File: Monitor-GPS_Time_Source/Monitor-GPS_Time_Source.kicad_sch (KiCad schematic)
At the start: 10 parts, among them J1 Conn_ARM_JTAG_SWD_10, J2 Conn_01x10_Pin, J3 Conn_01x10_Pin, SW1 SW_Omron_B3FS, U1 MSPM0C1105

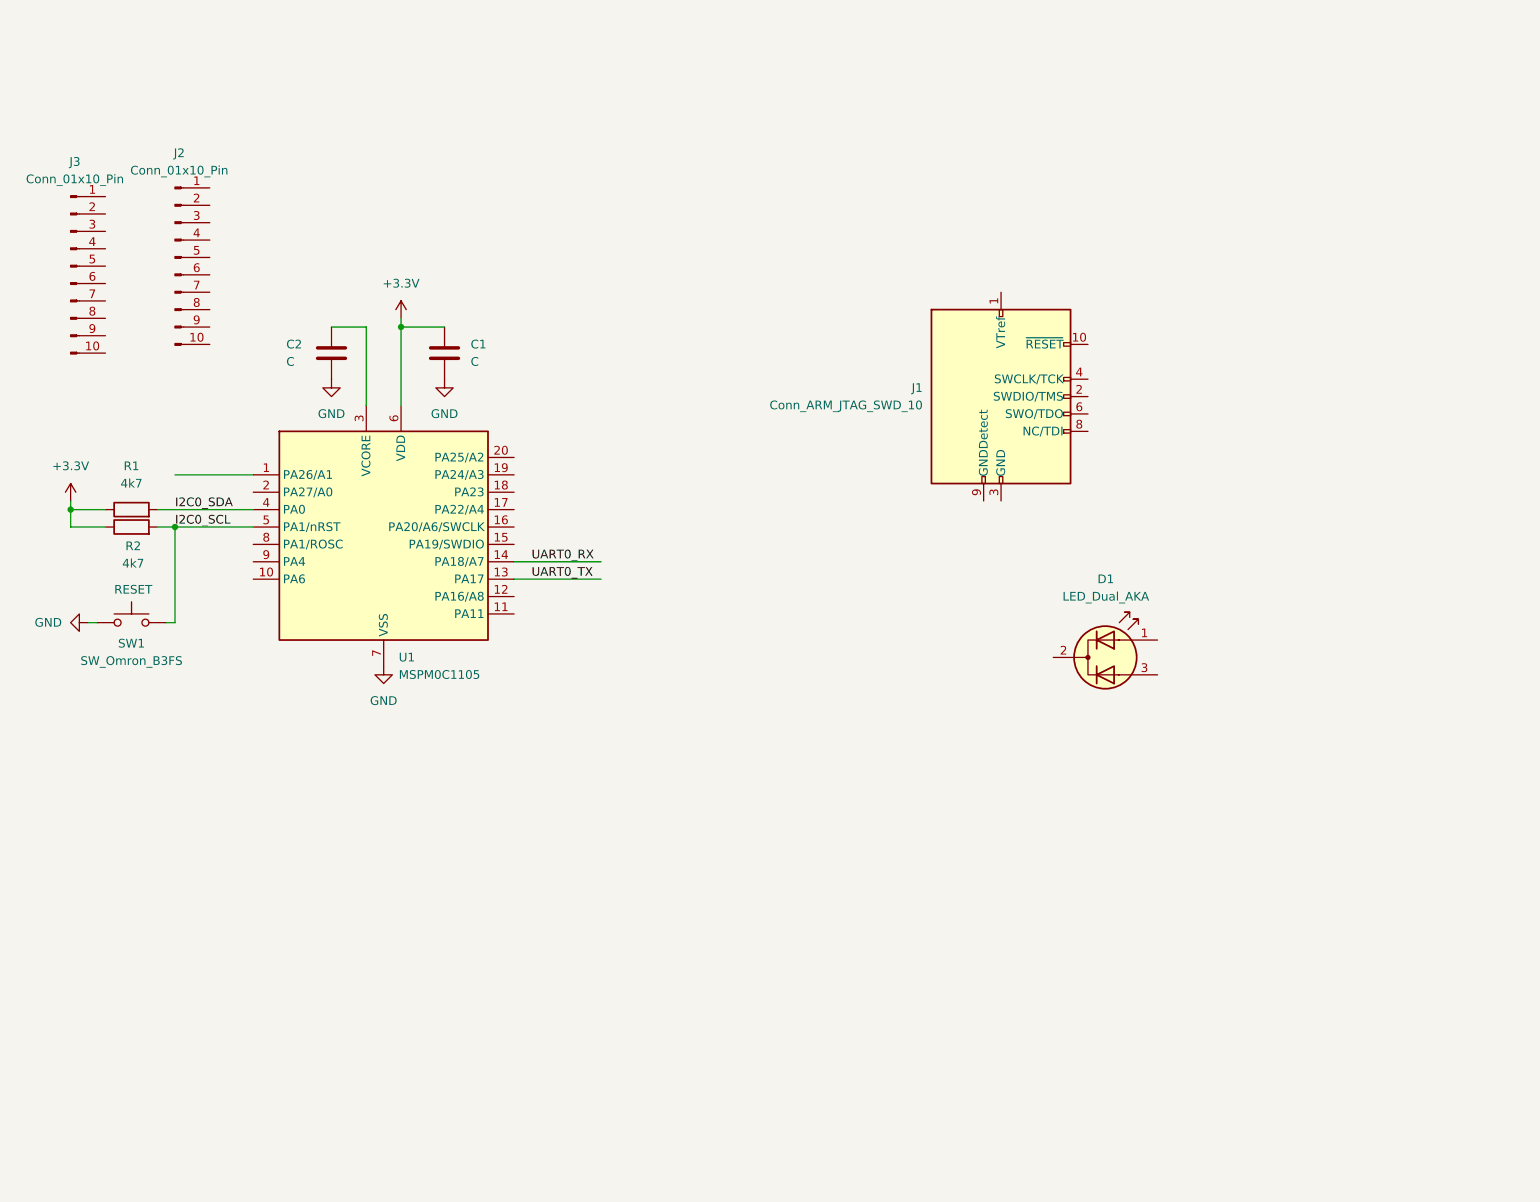
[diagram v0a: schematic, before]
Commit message: PCB layout complete, needs silkscreen work
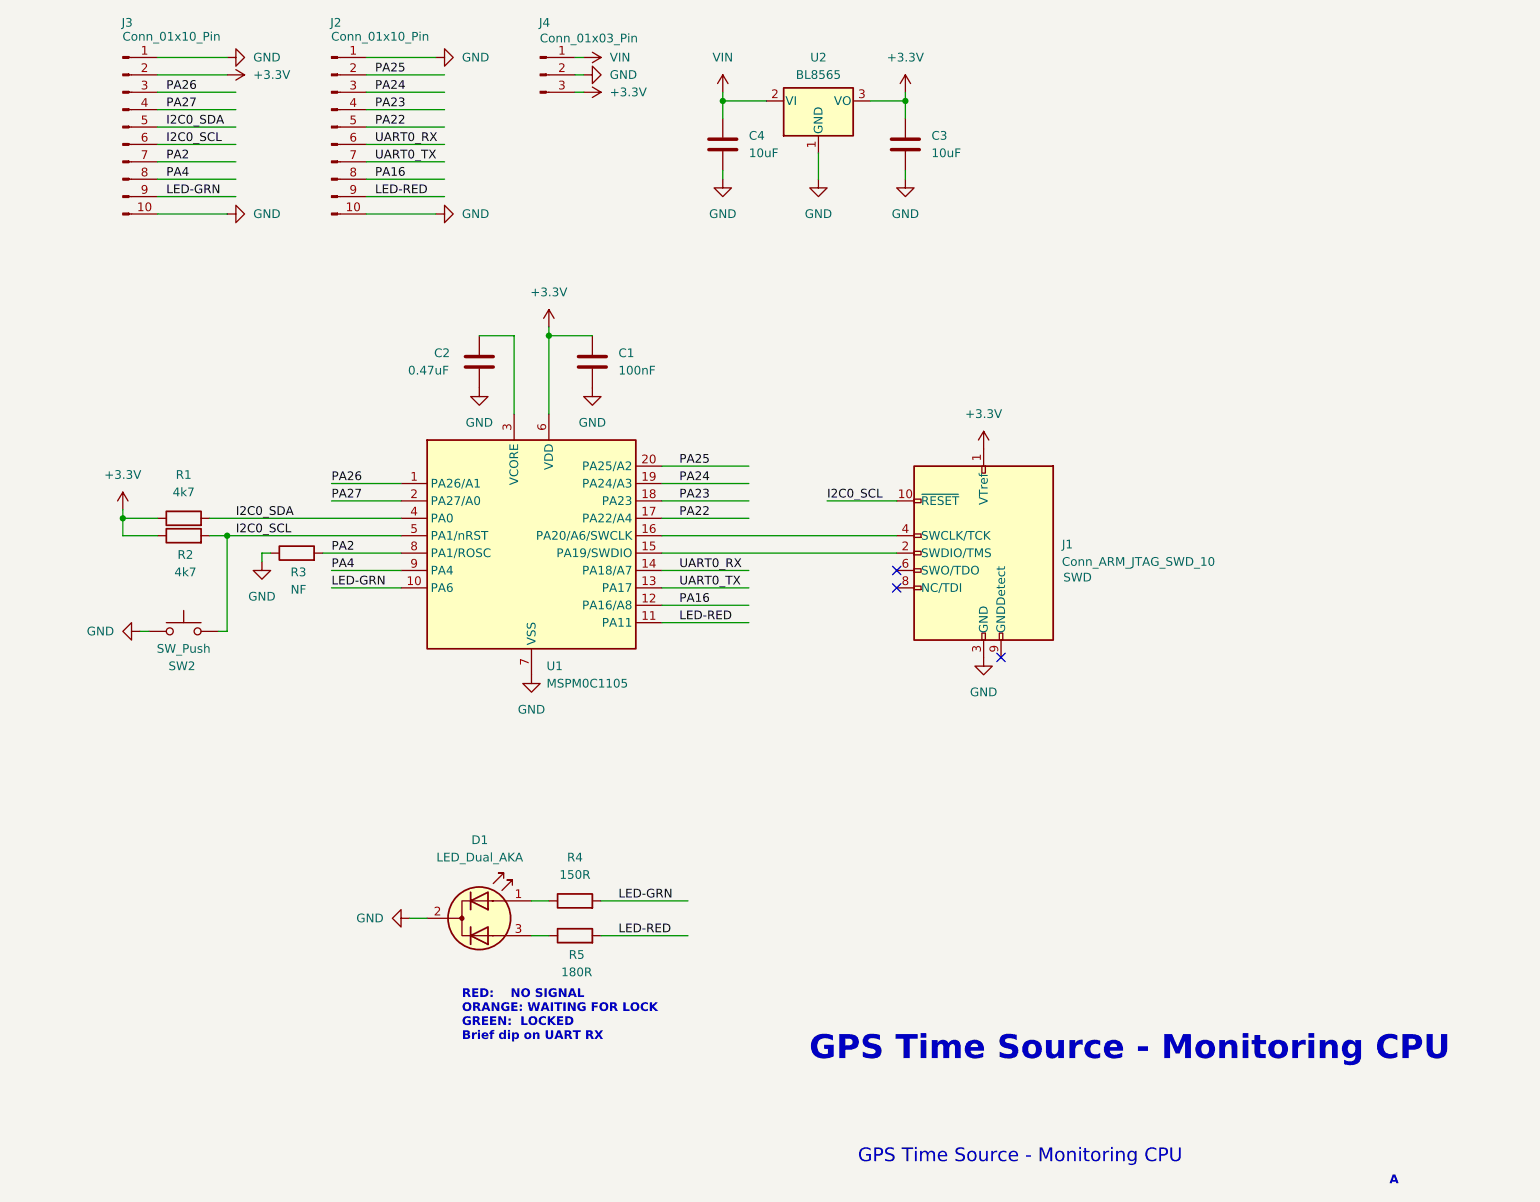
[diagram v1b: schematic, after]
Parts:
- removed SW1: SW_Omron_B3FS, Button_Switch_SMD:SW_SPST_Omron_B3FS-100xP, symbol Switch:SW_Omron_B3FS
- added C3, C4: 10uF, Capacitor_SMD:C_0805_2012Metric, symbol Device:C
- added J4: Conn_01x03_Pin, Connector_PinHeader_2.54mm:PinHeader_1x03_P2.54mm_Vertical, symbol Connector:Conn_01x03_Pin
- added R3: NF, Resistor_SMD:R_0603_1608Metric, symbol Device:R
- added R4: 150R, Resistor_SMD:R_0603_1608Metric, symbol Device:R
- added R5: 180R, Resistor_SMD:R_0603_1608Metric, symbol Device:R
- added SW2: SW_Push, Button_Switch_SMD:SW_Push_SPST_NO_Alps_SKRK, symbol Switch:SW_Push
- added U2: BL8565, Package_TO_SOT_SMD:SOT-223-3_TabPin2, symbol Regulator_Linear:AP2127R-3.3
- C1: value C -> 100nF
- C2: value C -> 0.47uF; footprint (none) -> Capacitor_SMD:C_0603_1608Metric
- J1: footprint (none) -> Connector_PinHeader_1.27mm:PinHeader_2x05_P1.27mm_Vertical_SMD; Function (none) -> SWD
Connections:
- net +3.3V: now also J1.1 (VTref), J3.2 (Pin_2), C3.1, J4.3 (Pin_3), U2.3 (VO)
- net GND: now also D1.2 (K), J1.3 (GND), J1.5 (GND), J2.1 (Pin_1), J2.10 (Pin_10), J3.1 (Pin_1), J3.10 (Pin_10), C3.2, C4.2, J4.2 (Pin_2), R3.1, SW2.1, U2.1 (GND)
- net I2C0_SCL: now also J1.10 (~{RESET}), J3.6 (Pin_6), SW2.2
- net I2C0_SDA: now also J3.5 (Pin_5)
- net UART0_RX: now also J2.6 (Pin_6)
- net UART0_TX: now also J2.7 (Pin_7)
- net PA26: now reaches J3.3 (Pin_3)
- net PA26: now also U1.1 (PA26/A1)
- net PA27: now reaches J3.4 (Pin_4)
- net PA27: now also U1.2 (PA27/A0)
- net PA2: now reaches J3.7 (Pin_7)
- net PA2: now also U1.8 (PA1/ROSC), R3.2
- net PA4: now reaches J3.8 (Pin_8)
- net PA4: now also U1.9 (PA4)
- net LED-GRN: now reaches J3.9 (Pin_9)
- net LED-GRN: now also U1.10 (PA6), R4.2
- net at D1.1 (A1): now also R4.1
- net at D1.3 (A2): now also R5.1
- net LED-RED: now reaches U1.11 (PA11)
- net LED-RED: now also J2.9 (Pin_9), R5.2
- net PA16: now reaches U1.12 (PA16/A8)
- net PA16: now also J2.8 (Pin_8)
- net at U1.15 (PA19/SWDIO): now also J1.2 (SWDIO/TMS)
- net at U1.16 (PA20/A6/SWCLK): now also J1.4 (SWCLK/TCK)
- net PA22: now reaches U1.17 (PA22/A4)
- net PA22: now also J2.5 (Pin_5)
- net PA23: now reaches U1.18 (PA23)
- net PA23: now also J2.4 (Pin_4)
- net PA24: now reaches U1.19 (PA24/A3)
- net PA24: now also J2.3 (Pin_3)
- net PA25: now reaches U1.20 (PA25/A2)
- net PA25: now also J2.2 (Pin_2)
- new net VIN: C4.1, J4.1 (Pin_1), U2.2 (VI)
- no-connect marks 0 -> 3
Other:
- note added: "A"
- note added: "GPS Time Source - Monitoring CPU"
- note added: "RED: NO SIGNAL ORANGE: WAITING FOR LOCK GREEN: LOCKED Brief dip on UART RX"
- moved on the sheet: C1, C2, D1, J1, J2, J3, R1, R2, U1

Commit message: Update code to match PCB rev A (was EVB). Minor sch corrections
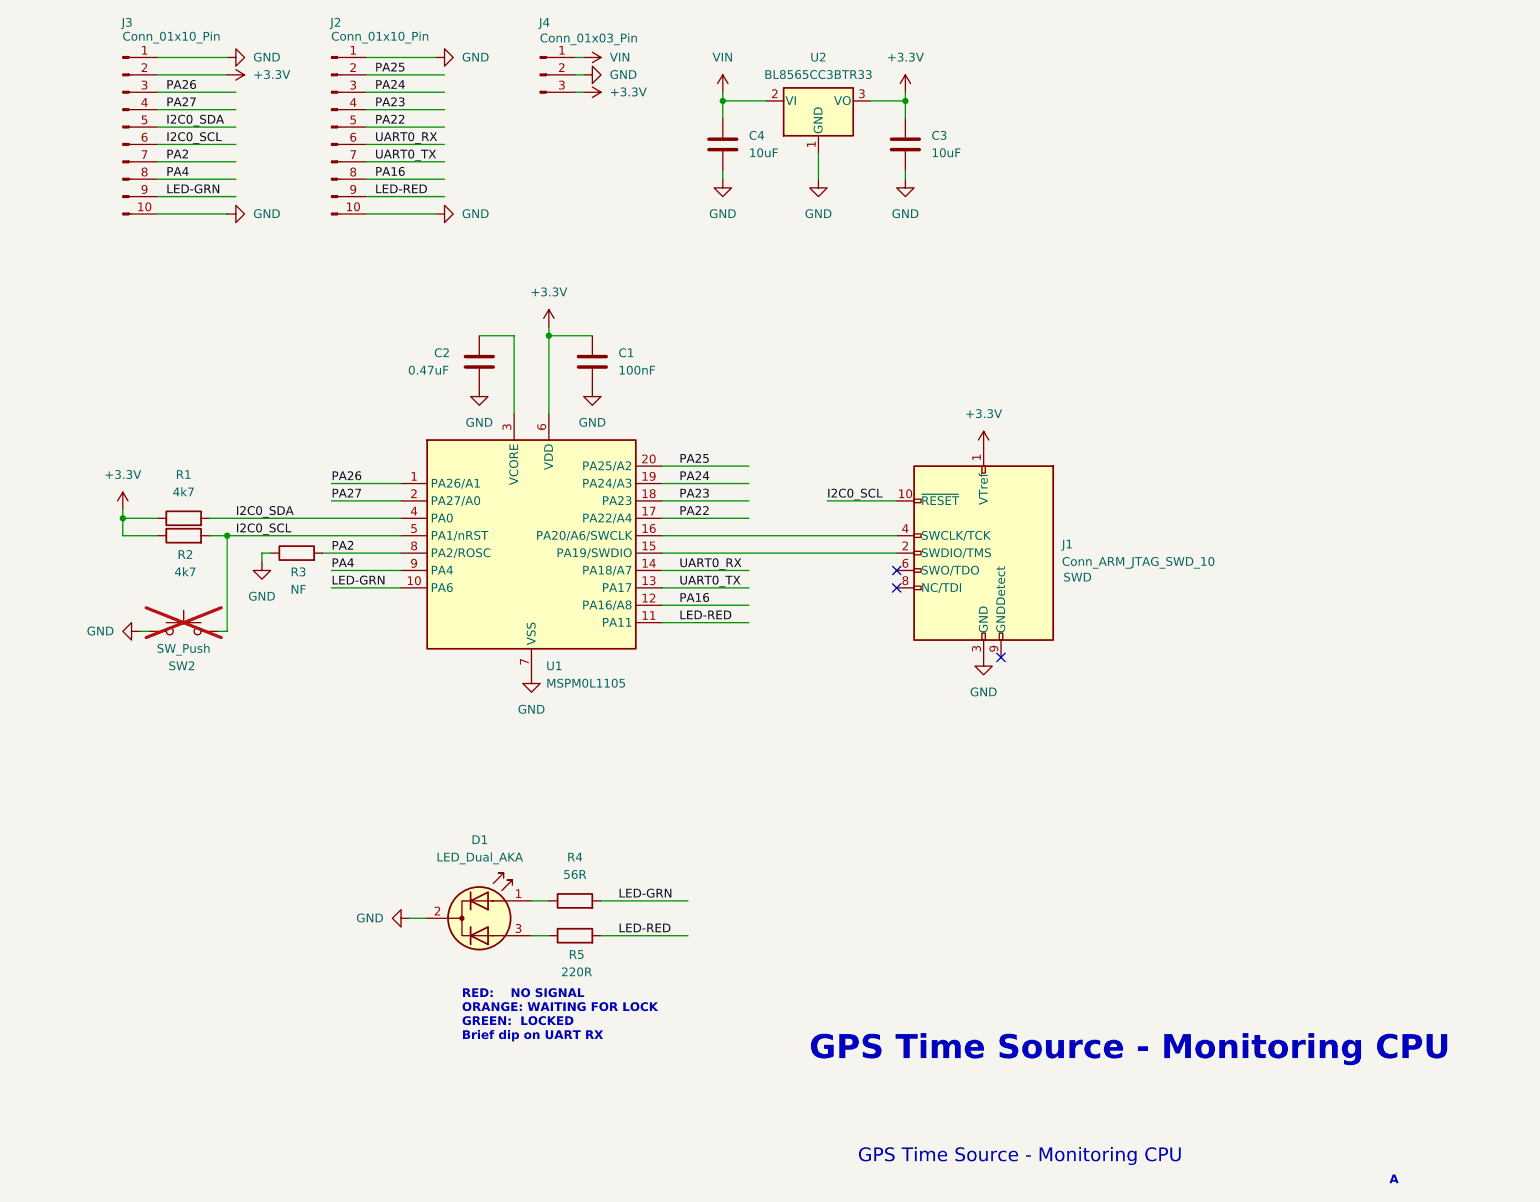
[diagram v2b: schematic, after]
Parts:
- R4: value 150R -> 56R
- R5: value 180R -> 220R
- SW2: now not fitted
- U1: value MSPM0C1105 -> MSPM0L1105
- U2: value BL8565 -> BL8565CC3BTR33; footprint Package_TO_SOT_SMD:SOT-223-3_TabPin2 -> Package_TO_SOT_SMD:SOT-89-3
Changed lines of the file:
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@@
 (kicad_sch
-	(version 20231120)
+	(version 20250114)
 	(generator "eeschema")
-	(generator_version "8.0")
+	(generator_version "9.0")
 	(paper "A4")
+	(text "GPS Time Source - Monitoring CPU"
+		(exclude_from_sim no)
+		(at 214.884 189.738 0)
+		(effects
+			(font
+				(size 2 2)
+				(thickness 0.25)
+			)
+		)
+	)
+	(text "GPS Time Source - Monitoring CPU"
+		(exclude_from_sim no)
+		(at 230.886 173.99 0)
+		(effects
+			(font
+				(size 3.5 3.5)
+				(thickness 0.6)
+				(bold yes)
+			)
+		)
+	)
+	(text "A"
+		(exclude_from_sim no)
+		(at 269.494 193.294 0)
+		(effects
+			(font
+				(size 1.27 1.27)
+				(thickness 0.254)
+				(bold yes)
+			)
+		)
+	)
+	(text "RED:    NO SIGNAL\nORANGE: WAITING FOR LOCK\nGREEN:  LOCKED\nBrief dip on UART RX"
+		(exclude_from_sim no)
+		(at 133.35 169.164 0)
+		(effects
+			(font
+				(face "Courier New")
+				(size 1.27 1.27)
+				(thickness 0.254)
+				(bold yes)
+			)
+			(justify left)
+		)
+	)
 	(junction
 		(at 99.06 99.06)
@@
 		)
 	)
-	(text "GPS Time Source - Monitoring CPU"
-		(exclude_from_sim no)
-		(at 214.884 189.738 0)
-		(effects
-			(font
-				(size 2 2)
-				(thickness 0.25)
-			)
-		)
-	)
-	(text "GPS Time Source - Monitoring CPU"
-		(exclude_from_sim no)
-		(at 230.886 173.99 0)
-		(effects
-			(font
-				(size 3.5 3.5)
-				(thickness 0.6)
-				(bold yes)
-			)
-		)
-	)
-	(text "A"
-		(exclude_from_sim no)
-		(at 269.494 193.294 0)
-		(effects
-			(font
-				(size 1.27 1.27)
-				(thickness 0.254)
-				(bold yes)
-			)
-		)
-	)
-	(text "RED:    NO SIGNAL\nORANGE: WAITING FOR LOCK\nGREEN:  LOCKED\nBrief dip on UART RX"
-		(exclude_from_sim no)
-		(at 133.35 169.164 0)
-		(effects
-			(font
-				(face "Courier New")
-				(size 1.27 1.27)
-				(thickness 0.254)
-				(bold yes)
-			)
-			(justify left)
-		)
-	)
 	(label "PA23"
 		(at 120.65 36.83 0)
-		(fields_autoplaced yes)
 		(effects
 			(font
@@
 	(label "LED-RED"
 		(at 120.65 49.53 0)
-		(fields_autoplaced yes)
 		(effects
 			(font
@@
 	(label "UART0_RX"
 		(at 165.1 104.14 0)
-		(fields_autoplaced yes)
 		(effects
 			(font
@@
 	(label "LED-GRN"
 		(at 156.21 152.4 0)
-		(fields_autoplaced yes)
 		(effects
 			(font
@@
 	(label "PA24"
 		(at 165.1 91.44 0)
-		(fields_autoplaced yes)
 		(effects
 			(font
@@
 	(label "PA16"
 		(at 165.1 109.22 0)
-		(fields_autoplaced yes)
 		(effects
 			(font
@@
 	(label "I2C0_SCL"
 		(at 100.33 99.06 0)
-		(fields_autoplaced yes)
 		(effects
 			(font
@@
 	(label "I2C0_SDA"
 		(at 90.17 39.37 0)
-		(fields_autoplaced yes)
 		(effects
 			(font
@@
 	(label "LED-RED"
 		(at 165.1 111.76 0)
-		(fields_autoplaced yes)
 		(effects
 			(font
@@
 	(label "PA26"
 		(at 90.17 34.29 0)
-		(fields_autoplaced yes)
 		(effects
 			(font
@@
 	(label "PA22"
 		(at 120.65 39.37 0)
-		(fields_autoplaced yes)
 		(effects
 			(font
@@
 	(label "PA16"
 		(at 120.65 46.99 0)
-		(fields_autoplaced yes)
 		(effects
 			(font
@@
 	(label "UART0_TX"
 		(at 120.65 44.45 0)
-		(fields_autoplaced yes)
 		(effects
 			(font
@@
 	(label "PA27"
 		(at 114.3 93.98 0)
-		(fields_autoplaced yes)
 		(effects
 			(font
@@
 	(label "I2C0_SDA"
 		(at 100.33 96.52 0)
-		(fields_autoplaced yes)
 		(effects
 			(font
@@
 	(label "PA24"
 		(at 120.65 34.29 0)
-		(fields_autoplaced yes)
 		(effects
 			(font
@@
 	(label "PA4"
 		(at 90.17 46.99 0)
-		(fields_autoplaced yes)
 		(effects
 			(font
@@
 	(label "I2C0_SCL"
 		(at 186.69 93.98 0)
-		(fields_autoplaced yes)
 		(effects
 			(font
@@
 	(label "PA2"
 		(at 114.3 101.6 0)
-		(fields_autoplaced yes)
 		(effects
 			(font
@@
 	(label "PA26"
 		(at 114.3 91.44 0)
-		(fields_autoplaced yes)
 		(effects
 			(font
@@
 	(label "LED-GRN"
 		(at 90.17 49.53 0)
-		(fields_autoplaced yes)
 		(effects
 			(font
@@
 	(label "PA25"
 		(at 120.65 31.75 0)
-		(fields_autoplaced yes)
 		(effects
 			(font
@@
 	(label "PA23"
 		(at 165.1 93.98 0)
-		(fields_autoplaced yes)
 		(effects
 			(font
@@
 	(label "PA4"
 		(at 114.3 104.14 0)
-		(fields_autoplaced yes)
 		(effects
 			(font
@@
 	(label "LED-RED"
 		(at 156.21 157.48 0)
-		(fields_autoplaced yes)
 		(effects
 			(font
@@
 	(label "PA2"
 		(at 90.17 44.45 0)
-		(fields_autoplaced yes)
 		(effects
 			(font
@@
 	(label "PA22"
 		(at 165.1 96.52 0)
-		(fields_autoplaced yes)
 		(effects
 			(font
@@
 	(label "PA27"
 		(at 90.17 36.83 0)
-		(fields_autoplaced yes)
 		(effects
 			(font
@@
 	(label "UART0_TX"
 		(at 165.1 106.68 0)
-		(fields_autoplaced yes)
 		(effects
 			(font
@@
 	(label "LED-GRN"
 		(at 114.3 106.68 0)
-		(fields_autoplaced yes)
 		(effects
 			(font
@@
 	(label "PA25"
 		(at 165.1 88.9 0)
-		(fields_autoplaced yes)
 		(effects
 			(font
@@
 	(label "UART0_RX"
 		(at 120.65 41.91 0)
-		(fields_autoplaced yes)
 		(effects
 			(font
@@
 	(label "I2C0_SCL"
 		(at 90.17 41.91 0)
-		(fields_autoplaced yes)
 		(effects
 			(font
@@
 			)
 		)
-		(property "Value" "BL8565"
+		(property "Value" "BL8565CC3BTR33"
 			(at 185.42 31.75 0)
 			(effects
@@
 			)
 		)
-		(property "Footprint" "Package_TO_SOT_SMD:SOT-223-3_TabPin2"
+		(property "Footprint" "Package_TO_SOT_SMD:SOT-89-3"
 			(at 185.42 30.48 0)
 			(effects
@@
 		(fields_autoplaced yes)
 		(property "Reference" "U1"
-			(at 145.7041 118.11 0)
+			(at 145.6533 118.11 0)
 			(effects
 				(font
@@
 			)
 		)
-		(property "Value" "MSPM0C1105"
-			(at 145.7041 120.65 0)
+		(property "Value" "MSPM0L1105"
+			(at 145.6533 120.65 0)
 			(effects
 				(font
@@
 			)
 		)
-		(property "Value" "150R"
+		(property "Value" "56R"
 			(at 149.86 148.59 90)
 			(effects
@@
 			)
 		)
-		(property "Value" "180R"
+		(property "Value" "220R"
 			(at 150.114 162.814 90)
 			(effects
@@
 		(in_bom yes)
 		(on_board yes)
-		(dnp no)
+		(dnp yes)
 		(property "Reference" "SW2"
 			(at 92.456 118.11 0)
@@
 		)
 	)
+	(embedded_fonts no)
 )
